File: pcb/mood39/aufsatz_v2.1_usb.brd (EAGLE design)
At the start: 16 x 11 mm, 8 parts

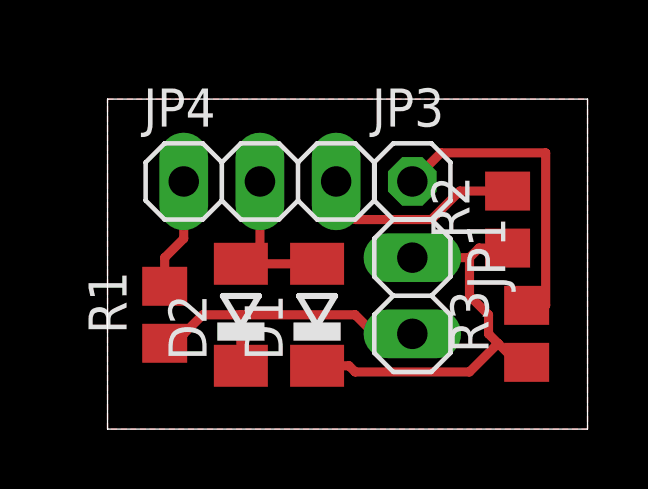
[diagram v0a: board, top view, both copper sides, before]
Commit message: optimize usb add-on board
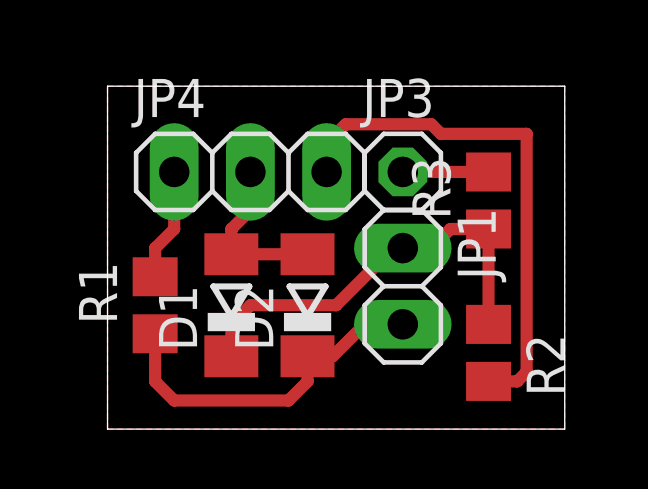
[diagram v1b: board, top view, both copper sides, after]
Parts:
- moved R3 4.62 mm to (12.7, 7.62)
- moved R2 4.49 mm to (12.7, 2.54), turned to 270 degrees
- moved D1 2.88 mm to (4.13, 4.13)
- moved D2 2.25 mm to (6.67, 4.13)
- moved JP1 0.45 mm to (9.84, 4.76)
- moved R1 0.45 mm to (1.59, 4.13)
- moved JP3 0.45 mm to (9.84, 8.57)
- moved JP4 0.45 mm to (4.76, 8.57)
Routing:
- net SCK: track 7.01 -> 17.4 mm
- net VCC: track 10.6 -> 3.49 mm
- net USBD+: track 10.6 -> 11.7 mm
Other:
- board size 16 x 11 mm -> 15.2 x 11.4 mm
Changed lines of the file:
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@@
 <board>
 <plain>
-<wire x1="0" y1="0" x2="16" y2="0" width="0" layer="20"/>
-<wire x1="16" y1="0" x2="16" y2="11" width="0" layer="20"/>
-<wire x1="16" y1="11" x2="0" y2="11" width="0" layer="20"/>
-<wire x1="0" y1="11" x2="0" y2="0" width="0" layer="20"/>
+<wire x1="0" y1="0" x2="15.24" y2="0" width="0" layer="20"/>
+<wire x1="15.24" y1="0" x2="15.24" y2="11.43" width="0" layer="20"/>
+<wire x1="15.24" y1="11.43" x2="0" y2="11.43" width="0" layer="20"/>
+<wire x1="0" y1="11.43" x2="0" y2="0" width="0" layer="20"/>
 </plain>
 <attributes>
@@
 </autorouter>
 <elements>
-<element name="JP1" library="pinhead" package="1X02" value="" x="10.16" y="4.445" rot="R270"/>
-<element name="R1" library="rcl" package="R0805" value="68R" x="1.905" y="3.81" rot="R90"/>
-<element name="R2" library="rcl" package="R0805" value="68R" x="13.335" y="6.985" rot="R90"/>
-<element name="R3" library="rcl" package="R0805" value="1k5" x="13.97" y="3.175" rot="R90"/>
-<element name="D1" library="diode" package="SOD80C" value="3V6" x="6.985" y="3.81" rot="R90"/>
-<element name="D2" library="diode" package="SOD80C" value="3V6" x="4.445" y="3.81" rot="R90"/>
-<element name="JP3" library="pinhead" package="1X01" value="" x="10.16" y="8.255"/>
-<element name="JP4" library="pinhead" package="1X03" value="" x="5.08" y="8.255"/>
+<element name="JP1" library="pinhead" package="1X02" value="" x="9.8425" y="4.7625" rot="R270"/>
+<element name="R1" library="rcl" package="R0805" value="68R" x="1.5875" y="4.1275" rot="R90"/>
+<element name="R2" library="rcl" package="R0805" value="68R" x="12.7" y="2.54" rot="R270"/>
+<element name="R3" library="rcl" package="R0805" value="1k5" x="12.7" y="7.62" rot="R90"/>
+<element name="D1" library="diode" package="SOD80C" value="3V6" x="4.1275" y="4.1275" rot="R90"/>
+<element name="D2" library="diode" package="SOD80C" value="3V6" x="6.6675" y="4.1275" rot="R90"/>
+<element name="JP3" library="pinhead" package="1X01" value="" x="9.8425" y="8.5725"/>
+<element name="JP4" library="pinhead" package="1X03" value="" x="4.7625" y="8.5725"/>
 </elements>
 <signals>
@@
 <contactref element="R1" pad="2"/>
 <contactref element="JP4" pad="1"/>
-<wire x1="2.54" y1="8.255" x2="2.54" y2="6.35" width="0.3048" layer="1"/>
-<wire x1="2.54" y1="6.35" x2="1.905" y2="5.715" width="0.3048" layer="1"/>
-<wire x1="1.905" y1="5.715" x2="1.905" y2="4.76" width="0.3048" layer="1"/>
+<wire x1="1.5875" y1="5.0775" x2="1.5875" y2="6.0325" width="0.4064" layer="1"/>
+<wire x1="1.5875" y1="6.0325" x2="2.2225" y2="6.6675" width="0.4064" layer="1"/>
+<wire x1="2.2225" y1="6.6675" x2="2.2225" y2="8.5725" width="0.4064" layer="1"/>
 </signal>
 <signal name="GND">
@@
 <contactref element="D1" pad="A"/>
 <contactref element="JP4" pad="2"/>
-<wire x1="4.445" y1="5.51" x2="5.08" y2="5.51" width="0.3048" layer="1"/>
-<wire x1="5.08" y1="5.51" x2="6.985" y2="5.51" width="0.3048" layer="1"/>
-<wire x1="5.08" y1="8.255" x2="5.08" y2="5.51" width="0.3048" layer="1"/>
-<polygon width="0.3048" layer="1" thermals="no">
-<vertex x="0" y="11"/>
-<vertex x="16" y="11"/>
-<vertex x="16" y="0"/>
+<wire x1="4.1275" y1="5.8275" x2="6.6675" y2="5.8275" width="0.4064" layer="1"/>
+<wire x1="4.7625" y1="8.5725" x2="4.7625" y2="7.3025" width="0.4064" layer="1"/>
+<wire x1="4.7625" y1="7.3025" x2="4.1275" y2="6.6675" width="0.4064" layer="1"/>
+<wire x1="4.1275" y1="6.6675" x2="4.1275" y2="5.8275" width="0.4064" layer="1"/>
+<polygon width="0.4064" layer="1" thermals="no">
+<vertex x="0" y="11.43"/>
+<vertex x="15.24" y="11.43"/>
+<vertex x="15.24" y="0"/>
 <vertex x="0" y="0"/>
 </polygon>
@@
 <contactref element="R2" pad="2"/>
 <contactref element="JP4" pad="3"/>
-<wire x1="13.335" y1="7.935" x2="11.745" y2="7.935" width="0.3048" layer="1"/>
-<wire x1="11.745" y1="7.935" x2="10.795" y2="6.985" width="0.3048" layer="1"/>
-<wire x1="10.795" y1="6.985" x2="8.255" y2="6.985" width="0.3048" layer="1"/>
-<wire x1="8.255" y1="6.985" x2="7.62" y2="7.62" width="0.3048" layer="1"/>
-<wire x1="7.62" y1="7.62" x2="7.62" y2="8.255" width="0.3048" layer="1"/>
+<wire x1="12.7" y1="1.59" x2="13.655" y2="1.59" width="0.4064" layer="1"/>
+<wire x1="13.655" y1="1.59" x2="13.97" y2="1.905" width="0.4064" layer="1"/>
+<wire x1="13.97" y1="1.905" x2="13.97" y2="9.8425" width="0.4064" layer="1"/>
+<wire x1="13.97" y1="9.8425" x2="11.1125" y2="9.8425" width="0.4064" layer="1"/>
+<wire x1="11.1125" y1="9.8425" x2="10.795" y2="10.16" width="0.4064" layer="1"/>
+<wire x1="10.795" y1="10.16" x2="7.9375" y2="10.16" width="0.4064" layer="1"/>
+<wire x1="7.9375" y1="10.16" x2="7.3025" y2="9.525" width="0.4064" layer="1"/>
+<wire x1="7.3025" y1="9.525" x2="7.3025" y2="8.5725" width="0.4064" layer="1"/>
 </signal>
 <signal name="VCC">
 <contactref element="R3" pad="2"/>
 <contactref element="JP3" pad="1"/>
-<wire x1="13.97" y1="4.125" x2="14.605" y2="4.125" width="0.3048" layer="1"/>
-<wire x1="14.605" y1="4.125" x2="14.605" y2="9.2075" width="0.3048" layer="1"/>
-<wire x1="14.605" y1="9.2075" x2="11.1125" y2="9.2075" width="0.3048" layer="1"/>
-<wire x1="11.1125" y1="9.2075" x2="10.16" y2="8.255" width="0.3048" layer="1"/>
+<wire x1="12.7" y1="8.57" x2="13.015" y2="8.5725" width="0.4064" layer="1"/>
+<wire x1="13.015" y1="8.5725" x2="9.8425" y2="8.5725" width="0.4064" layer="1"/>
 </signal>
 <signal name="USBD-">
@@
 <contactref element="R3" pad="1"/>
 <contactref element="D1" pad="C"/>
-<wire x1="13.335" y1="6.035" x2="12.385" y2="6.035" width="0.3048" layer="1"/>
-<wire x1="12.385" y1="6.035" x2="12.065" y2="5.715" width="0.3048" layer="1"/>
-<wire x1="12.065" y1="5.715" x2="10.16" y2="5.715" width="0.3048" layer="1"/>
-<wire x1="13.97" y1="2.225" x2="13.65" y2="2.225" width="0.3048" layer="1"/>
-<wire x1="13.65" y1="2.225" x2="13.0175" y2="2.8575" width="0.3048" layer="1"/>
-<wire x1="6.985" y1="2.11" x2="8.05" y2="2.11" width="0.3048" layer="1"/>
-<wire x1="8.05" y1="2.11" x2="8.255" y2="1.905" width="0.3048" layer="1"/>
-<wire x1="8.255" y1="1.905" x2="12.065" y2="1.905" width="0.3048" layer="1"/>
-<wire x1="12.065" y1="1.905" x2="13.0175" y2="2.8575" width="0.3048" layer="1"/>
-<wire x1="13.0175" y1="2.8575" x2="12.7" y2="3.175" width="0.3048" layer="1"/>
-<wire x1="12.7" y1="3.175" x2="12.7" y2="3.81" width="0.3048" layer="1"/>
-<wire x1="12.7" y1="3.81" x2="12.065" y2="4.445" width="0.3048" layer="1"/>
-<wire x1="12.065" y1="4.445" x2="12.065" y2="5.715" width="0.3048" layer="1"/>
+<wire x1="4.1275" y1="2.4275" x2="4.1275" y2="3.4925" width="0.4064" layer="1"/>
+<wire x1="4.1275" y1="3.4925" x2="4.7625" y2="4.1275" width="0.4064" layer="1"/>
+<wire x1="4.7625" y1="4.1275" x2="7.62" y2="4.1275" width="0.4064" layer="1"/>
+<wire x1="7.62" y1="4.1275" x2="9.525" y2="6.0325" width="0.4064" layer="1"/>
+<wire x1="9.525" y1="6.0325" x2="9.8425" y2="6.0325" width="0.4064" layer="1"/>
+<wire x1="12.7" y1="6.67" x2="12.7" y2="3.49" width="0.4064" layer="1"/>
+<wire x1="12.7" y1="6.67" x2="11.4325" y2="6.67" width="0.4064" layer="1"/>
+<wire x1="11.4325" y1="6.67" x2="10.795" y2="6.0325" width="0.4064" layer="1"/>
+<wire x1="10.795" y1="6.0325" x2="9.8425" y2="6.0325" width="0.4064" layer="1"/>
 </signal>
 <signal name="USBD+">
@@
 <contactref element="R1" pad="1"/>
 <contactref element="D2" pad="C"/>
-<wire x1="10.16" y1="3.175" x2="8.89" y2="3.175" width="0.3048" layer="1"/>
-<wire x1="8.89" y1="3.175" x2="8.255" y2="3.81" width="0.3048" layer="1"/>
-<wire x1="8.255" y1="3.81" x2="4.445" y2="3.81" width="0.3048" layer="1"/>
-<wire x1="4.445" y1="3.81" x2="3.175" y2="3.81" width="0.3048" layer="1"/>
-<wire x1="3.175" y1="3.81" x2="2.54" y2="3.175" width="0.3048" layer="1"/>
-<wire x1="2.54" y1="3.175" x2="2.22" y2="3.175" width="0.3048" layer="1"/>
-<wire x1="2.22" y1="3.175" x2="1.905" y2="2.86" width="0.3048" layer="1"/>
-<wire x1="4.445" y1="2.11" x2="4.445" y2="3.81" width="0.3048" layer="1"/>
+<wire x1="6.6675" y1="2.4275" x2="6.6675" y2="1.5875" width="0.4064" layer="1"/>
+<wire x1="6.6675" y1="1.5875" x2="6.0325" y2="0.9525" width="0.4064" layer="1"/>
+<wire x1="6.0325" y1="0.9525" x2="2.2225" y2="0.9525" width="0.4064" layer="1"/>
+<wire x1="2.2225" y1="0.9525" x2="1.5875" y2="1.5875" width="0.4064" layer="1"/>
+<wire x1="1.5875" y1="1.5875" x2="1.5875" y2="3.1775" width="0.4064" layer="1"/>
+<wire x1="6.6675" y1="2.4275" x2="7.5075" y2="2.4275" width="0.4064" layer="1"/>
+<wire x1="7.5075" y1="2.4275" x2="8.5725" y2="3.4925" width="0.4064" layer="1"/>
+<wire x1="8.5725" y1="3.4925" x2="9.8425" y2="3.4925" width="0.4064" layer="1"/>
 </signal>
 </signals>
